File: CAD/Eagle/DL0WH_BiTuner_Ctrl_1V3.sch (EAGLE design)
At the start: 156 parts, among them Q0321 ABS07-32.768KHZ, U0101 STM32L476RGT6_64PIN_LDO, U0601 MC33996, U0701 MC33996, U0801 MC33996, U0921 TS5A23166, U0941 LM2611, U0951 OPA354, U0961 OPA354, U0962 MCP4661-103E-MS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

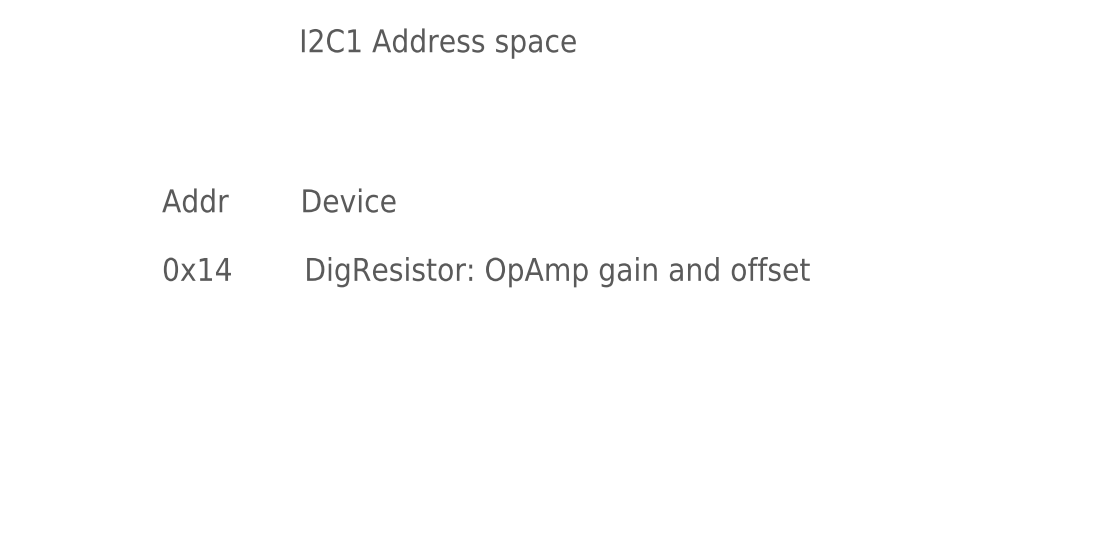
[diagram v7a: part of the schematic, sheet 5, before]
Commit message: HW_1V3 - CAD/Eagle - wrong I2C address fixed
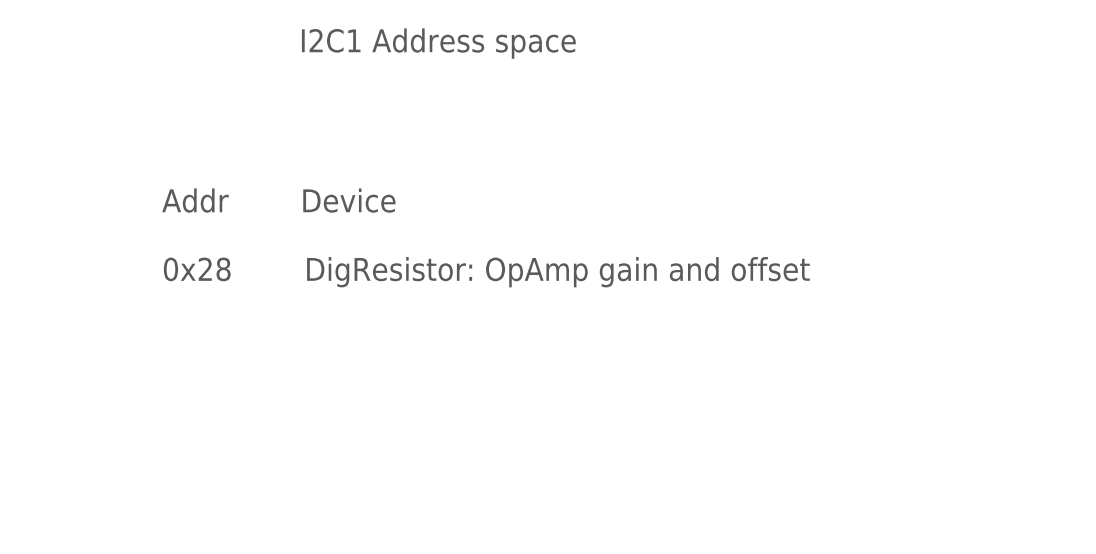
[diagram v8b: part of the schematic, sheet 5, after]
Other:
- note added: "Addr Device 0x28 DigResistor: OpAmp gain and offset"
- note removed: "Addr Device 0x14 DigResistor: OpAmp gain and offset"
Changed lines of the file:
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@@
 <plain>
 <text x="134.62" y="137.16" size="2.54" layer="97" ratio="15">Addr        Device
-0x14        DigResistor: OpAmp gain and offset
+0x28        DigResistor: OpAmp gain and offset
 </text>
 <text x="22.86" y="162.56" size="2.54" layer="97" ratio="15">I2C1 Termination</text>
